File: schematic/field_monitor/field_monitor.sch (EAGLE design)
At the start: 5 parts, among them Q1 MOSFET

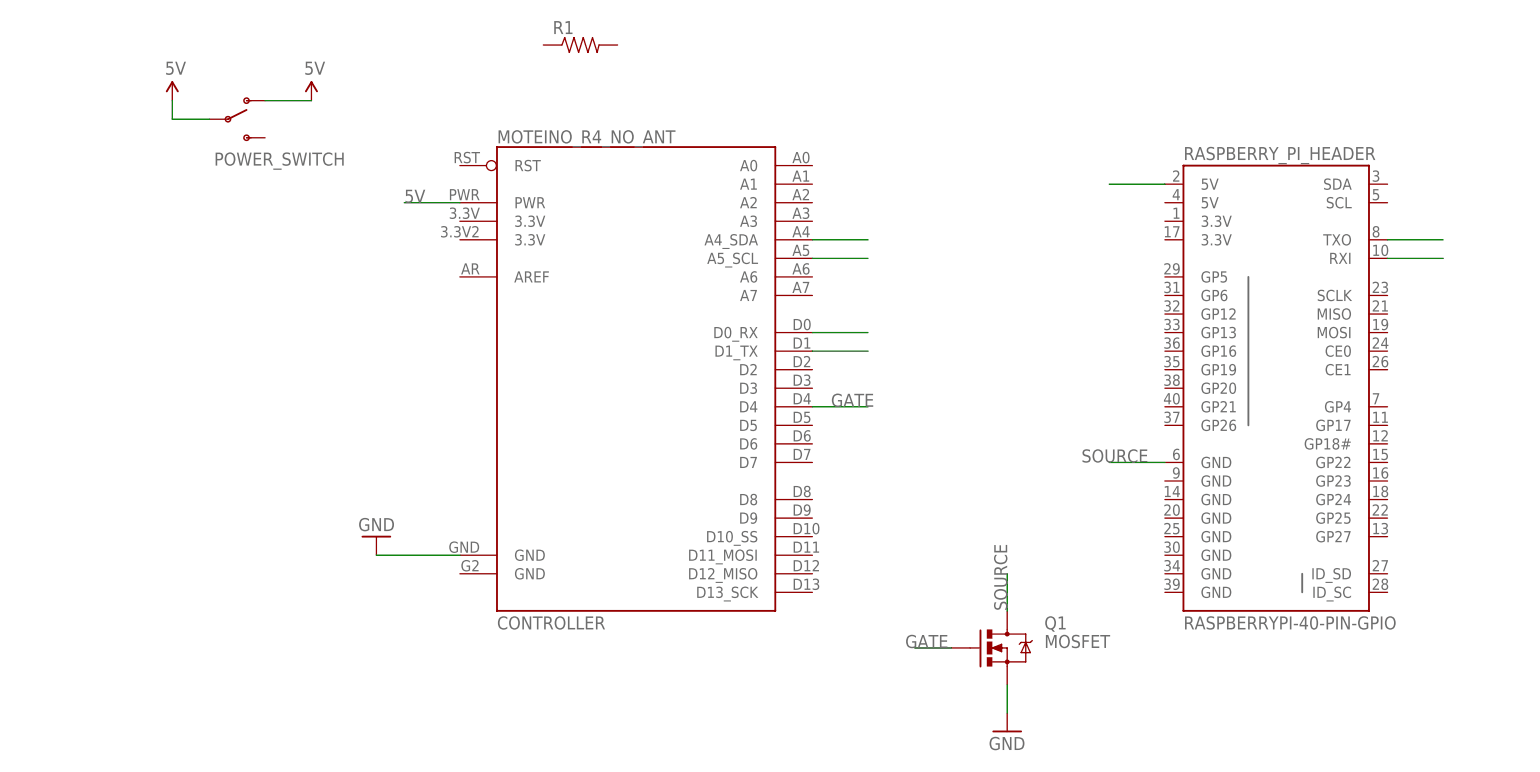
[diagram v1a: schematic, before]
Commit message: Added RTC to schematic
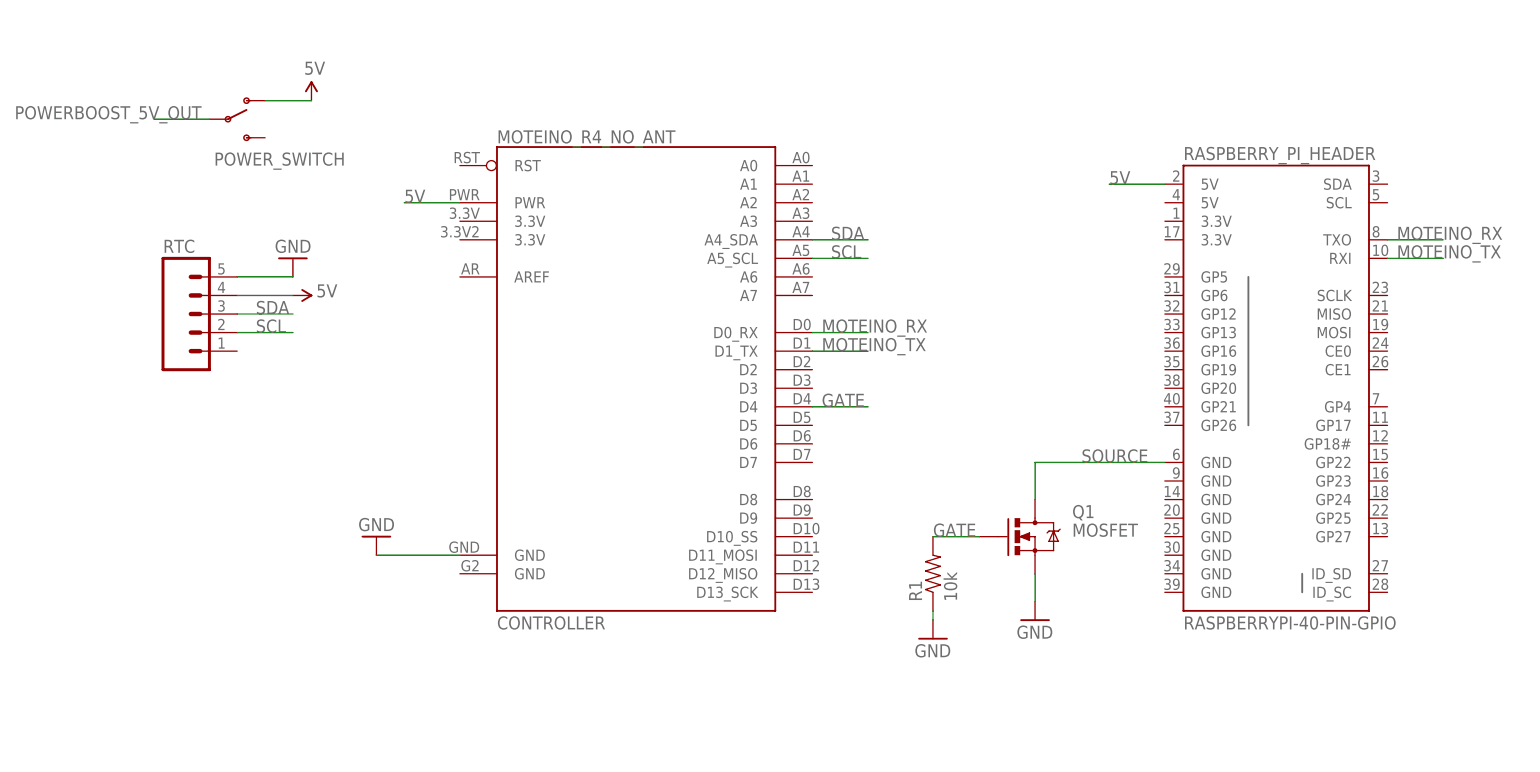
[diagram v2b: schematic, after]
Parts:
- added RTC: (no value), SparkFun-Connectors:M05PTH
- R1: value (none) -> 10k
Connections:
- removed net N$10: RASPBERRY_PI_HEADER.TXO
- removed net N$11: RASPBERRY_PI_HEADER.RXI
- removed net N$3: CONTROLLER.A5_SCL
- removed net N$4: CONTROLLER.A4_SDA
- removed net N$5: CONTROLLER.D0_RX
- removed net N$6: CONTROLLER.D1_TX
- new net MOTEINO_RX: CONTROLLER.D0_RX, RASPBERRY_PI_HEADER.TXO
- new net MOTEINO_TX: CONTROLLER.D1_TX, RASPBERRY_PI_HEADER.RXI
- new net POWERBOOST_5V_OUT: POWER_SWITCH.P
- new net SCL: CONTROLLER.A5_SCL, RTC.2
- new net SDA: CONTROLLER.A4_SDA, RTC.3
- net 5V: now also RTC.4; no longer POWER_SWITCH.P
- net GATE: now also R1.2
- net GND: now also R1.1, RTC.5
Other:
- moved on the sheet: Q1, R1
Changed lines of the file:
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@@
 <layer number="113" name="IDFDebug" color="7" fill="1" visible="yes" active="yes"/>
 <layer number="114" name="Badge_Outline" color="11" fill="1" visible="no" active="no"/>
+<layer number="115" name="ReferenceISLANDS" color="7" fill="1" visible="yes" active="yes"/>
 <layer number="116" name="Patch_BOT" color="7" fill="1" visible="yes" active="yes"/>
 <layer number="118" name="Rect_Pads" color="7" fill="1" visible="yes" active="yes"/>
@@
 <part name="CONTROLLER" library="MoteinoR4Mod" deviceset="MOTEINO_R4_NO_ANT" device=""/>
 <part name="Q1" library="SparkFun-DiscreteSemi" deviceset="MOSFET-NCHANNEL" device="FQP30N06L" value="MOSFET"/>
-<part name="R1" library="SparkFun-Passives" deviceset="RESISTOR" device="PTH-1/4W"/>
+<part name="R1" library="SparkFun-Passives" deviceset="RESISTOR" device="PTH-1/4W" value="10k"/>
 <part name="POWER_SWITCH" library="SparkFun-Electromechanical" deviceset="SWITCH-SPDT" device="PTH"/>
 <part name="RASPBERRY_PI_HEADER" library="SparkFun-Boards" deviceset="RASPBERRYPI-40-PIN-GPIO" device=""/>
-<part name="SUPPLY1" library="SparkFun-Aesthetics" deviceset="5V" device=""/>
 <part name="GND1" library="SparkFun-Aesthetics" deviceset="GND" device=""/>
 <part name="SUPPLY2" library="SparkFun-Aesthetics" deviceset="5V" device=""/>
 <part name="GND2" library="SparkFun-Aesthetics" deviceset="GND" device=""/>
+<part name="GND3" library="SparkFun-Aesthetics" deviceset="GND" device=""/>
+<part name="RTC" library="SparkFun-Connectors" deviceset="M05" device="PTH"/>
+<part name="GND4" library="SparkFun-Aesthetics" deviceset="GND" device=""/>
+<part name="SUPPLY3" library="SparkFun-Aesthetics" deviceset="5V" device=""/>
 </parts>
 <sheets>
@@
 <instances>
 <instance part="CONTROLLER" gate="G$1" x="71.12" y="48.26"/>
-<instance part="Q1" gate="G$1" x="120.65" y="7.62"/>
-<instance part="R1" gate="G$1" x="62.23" y="90.17"/>
+<instance part="Q1" gate="G$1" x="124.46" y="22.86"/>
+<instance part="R1" gate="G$1" x="110.49" y="17.78" rot="R90"/>
 <instance part="POWER_SWITCH" gate="1" x="13.97" y="80.01"/>
 <instance part="RASPBERRY_PI_HEADER" gate="G$1" x="157.48" y="45.72"/>
-<instance part="SUPPLY1" gate="G$1" x="6.35" y="82.55"/>
 <instance part="GND1" gate="1" x="34.29" y="22.86" rot="R180"/>
 <instance part="SUPPLY2" gate="G$1" x="25.4" y="82.55"/>
-<instance part="GND2" gate="1" x="120.65" y="-3.81"/>
+<instance part="GND2" gate="1" x="124.46" y="11.43"/>
+<instance part="GND3" gate="1" x="110.49" y="8.89"/>
+<instance part="RTC" gate="G$1" x="7.62" y="53.34"/>
+<instance part="GND4" gate="1" x="22.86" y="60.96" rot="R180"/>
+<instance part="SUPPLY3" gate="G$1" x="22.86" y="55.88" smashed="yes" rot="R270">
+<attribute name="VALUE" x="28.956" y="57.404" size="1.778" layer="96" rot="R180"/>
+</instance>
 </instances>
 <busses>
 </busses>
 <nets>
-<net name="N$3" class="0">
+<net name="SCL" class="0">
 <segment>
 <pinref part="CONTROLLER" gate="G$1" pin="A5_SCL"/>
 <wire x1="93.98" y1="60.96" x2="101.6" y2="60.96" width="0.1524" layer="91"/>
-</segment>
-</net>
-<net name="N$4" class="0">
+<label x="96.52" y="60.96" size="1.778" layer="95"/>
+</segment>
+<segment>
+<pinref part="RTC" gate="G$1" pin="2"/>
+<wire x1="15.24" y1="50.8" x2="22.86" y2="50.8" width="0.1524" layer="91"/>
+<label x="17.78" y="50.8" size="1.778" layer="95"/>
+</segment>
+</net>
+<net name="SDA" class="0">
 <segment>
 <pinref part="CONTROLLER" gate="G$1" pin="A4_SDA"/>
 <wire x1="93.98" y1="63.5" x2="101.6" y2="63.5" width="0.1524" layer="91"/>
-</segment>
-</net>
-<net name="N$5" class="0">
-<segment>
-<pinref part="CONTROLLER" gate="G$1" pin="D0_RX"/>
-<wire x1="93.98" y1="50.8" x2="101.6" y2="50.8" width="0.1524" layer="91"/>
-</segment>
-</net>
-<net name="N$6" class="0">
-<segment>
-<pinref part="CONTROLLER" gate="G$1" pin="D1_TX"/>
-<wire x1="93.98" y1="48.26" x2="101.6" y2="48.26" width="0.1524" layer="91"/>
-</segment>
-</net>
-<net name="N$10" class="0">
-<segment>
-<pinref part="RASPBERRY_PI_HEADER" gate="G$1" pin="TXO"/>
-<wire x1="172.72" y1="63.5" x2="180.34" y2="63.5" width="0.1524" layer="91"/>
-</segment>
-</net>
-<net name="N$11" class="0">
-<segment>
-<pinref part="RASPBERRY_PI_HEADER" gate="G$1" pin="RXI"/>
-<wire x1="172.72" y1="60.96" x2="180.34" y2="60.96" width="0.1524" layer="91"/>
+<label x="96.52" y="63.5" size="1.778" layer="95"/>
+</segment>
+<segment>
+<pinref part="RTC" gate="G$1" pin="3"/>
+<wire x1="15.24" y1="53.34" x2="22.86" y2="53.34" width="0.1524" layer="91"/>
+<label x="17.78" y="53.34" size="1.778" layer="95"/>
 </segment>
 </net>
 <net name="5V" class="0">
-<segment>
-<pinref part="SUPPLY1" gate="G$1" pin="5V"/>
-<wire x1="6.35" y1="82.55" x2="6.35" y2="80.01" width="0.1524" layer="91"/>
-<pinref part="POWER_SWITCH" gate="1" pin="P"/>
-<wire x1="6.35" y1="80.01" x2="11.43" y2="80.01" width="0.1524" layer="91"/>
-</segment>
 <segment>
 <pinref part="POWER_SWITCH" gate="1" pin="O"/>
@@
 <pinref part="RASPBERRY_PI_HEADER" gate="G$1" pin="5V@2"/>
 <wire x1="142.24" y1="71.12" x2="134.62" y2="71.12" width="0.1524" layer="91"/>
+<label x="134.62" y="71.12" size="1.778" layer="95"/>
+</segment>
+<segment>
+<pinref part="RTC" gate="G$1" pin="4"/>
+<wire x1="15.24" y1="55.88" x2="22.86" y2="55.88" width="0.1524" layer="91"/>
+<pinref part="SUPPLY3" gate="G$1" pin="5V"/>
 </segment>
 </net>
@@
 <segment>
 <pinref part="Q1" gate="G$1" pin="S"/>
-<wire x1="120.65" y1="2.54" x2="120.65" y2="-1.27" width="0.1524" layer="91"/>
+<wire x1="124.46" y1="17.78" x2="124.46" y2="13.97" width="0.1524" layer="91"/>
 <pinref part="GND2" gate="1" pin="GND"/>
 </segment>
+<segment>
+<pinref part="R1" gate="G$1" pin="1"/>
+<pinref part="GND3" gate="1" pin="GND"/>
+<wire x1="110.49" y1="12.7" x2="110.49" y2="11.43" width="0.1524" layer="91"/>
+</segment>
+<segment>
+<pinref part="RTC" gate="G$1" pin="5"/>
+<wire x1="15.24" y1="58.42" x2="22.86" y2="58.42" width="0.1524" layer="91"/>
+<pinref part="GND4" gate="1" pin="GND"/>
+</segment>
 </net>
 <net name="GATE" class="0">
 <segment>
 <pinref part="Q1" gate="G$1" pin="G"/>
-<wire x1="113.03" y1="7.62" x2="107.95" y2="7.62" width="0.1524" layer="91"/>
-<label x="106.68" y="7.62" size="1.778" layer="95"/>
+<wire x1="116.84" y1="22.86" x2="110.49" y2="22.86" width="0.1524" layer="91"/>
+<label x="110.49" y="22.86" size="1.778" layer="95"/>
+<pinref part="R1" gate="G$1" pin="2"/>
 </segment>
 <segment>
 <pinref part="CONTROLLER" gate="G$1" pin="D4"/>
 <wire x1="93.98" y1="40.64" x2="101.6" y2="40.64" width="0.1524" layer="91"/>
-<label x="96.52" y="40.64" size="1.778" layer="95"/>
+<label x="95.25" y="40.64" size="1.778" layer="95"/>
 </segment>
 </net>
@@
 <segment>
 <pinref part="RASPBERRY_PI_HEADER" gate="G$1" pin="GND@6"/>
-<wire x1="142.24" y1="33.02" x2="134.62" y2="33.02" width="0.1524" layer="91"/>
 <label x="130.81" y="33.02" size="1.778" layer="95"/>
-</segment>
-<segment>
 <pinref part="Q1" gate="G$1" pin="D"/>
-<wire x1="120.65" y1="12.7" x2="120.65" y2="17.78" width="0.1524" layer="91"/>
-<label x="120.65" y="12.7" size="1.778" layer="95" rot="R90"/>
-</segment>
-</net>
+<wire x1="124.46" y1="27.94" x2="124.46" y2="33.02" width="0.1524" layer="91"/>
+<wire x1="142.24" y1="33.02" x2="124.46" y2="33.02" width="0.1524" layer="91"/>
+</segment>
+</net>
+<net name="MOTEINO_RX" class="0">
+<segment>
+<pinref part="CONTROLLER" gate="G$1" pin="D0_RX"/>
+<wire x1="93.98" y1="50.8" x2="101.6" y2="50.8" width="0.1524" layer="91"/>
+<label x="95.25" y="50.8" size="1.778" layer="95"/>
+</segment>
+<segment>
+<pinref part="RASPBERRY_PI_HEADER" gate="G$1" pin="TXO"/>
+<wire x1="172.72" y1="63.5" x2="180.34" y2="63.5" width="0.1524" layer="91"/>
+<label x="173.99" y="63.5" size="1.778" layer="95"/>
+</segment>
+</net>
+<net name="MOTEINO_TX" class="0">
+<segment>
+<pinref part="CONTROLLER" gate="G$1" pin="D1_TX"/>
+<wire x1="93.98" y1="48.26" x2="101.6" y2="48.26" width="0.1524" layer="91"/>
+<label x="95.25" y="48.26" size="1.778" layer="95"/>
+</segment>
+<segment>
+<pinref part="RASPBERRY_PI_HEADER" gate="G$1" pin="RXI"/>
+<wire x1="172.72" y1="60.96" x2="180.34" y2="60.96" width="0.1524" layer="91"/>
+<label x="173.99" y="60.96" size="1.778" layer="95"/>
+</segment>
+</net>
+<net name="POWERBOOST_5V_OUT" class="0">
+<segment>
+<pinref part="POWER_SWITCH" gate="1" pin="P"/>
+<wire x1="11.43" y1="80.01" x2="3.81" y2="80.01" width="0.1524" layer="91"/>
+<label x="-15.24" y="80.01" size="1.778" layer="95"/>
+</segment>
+</net>
